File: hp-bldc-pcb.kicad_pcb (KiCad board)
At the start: 4 copper layers, 96 x 53 mm, 596 parts, among them IC101 MCP1790-5002E/DB, IC401 PIC16F1936, IC601 BTN8962TA, IC631 BTN8962TA, IC661 BTN8962TA, T102 SBC817-40LT1G, T103 SBC817-40LT1G

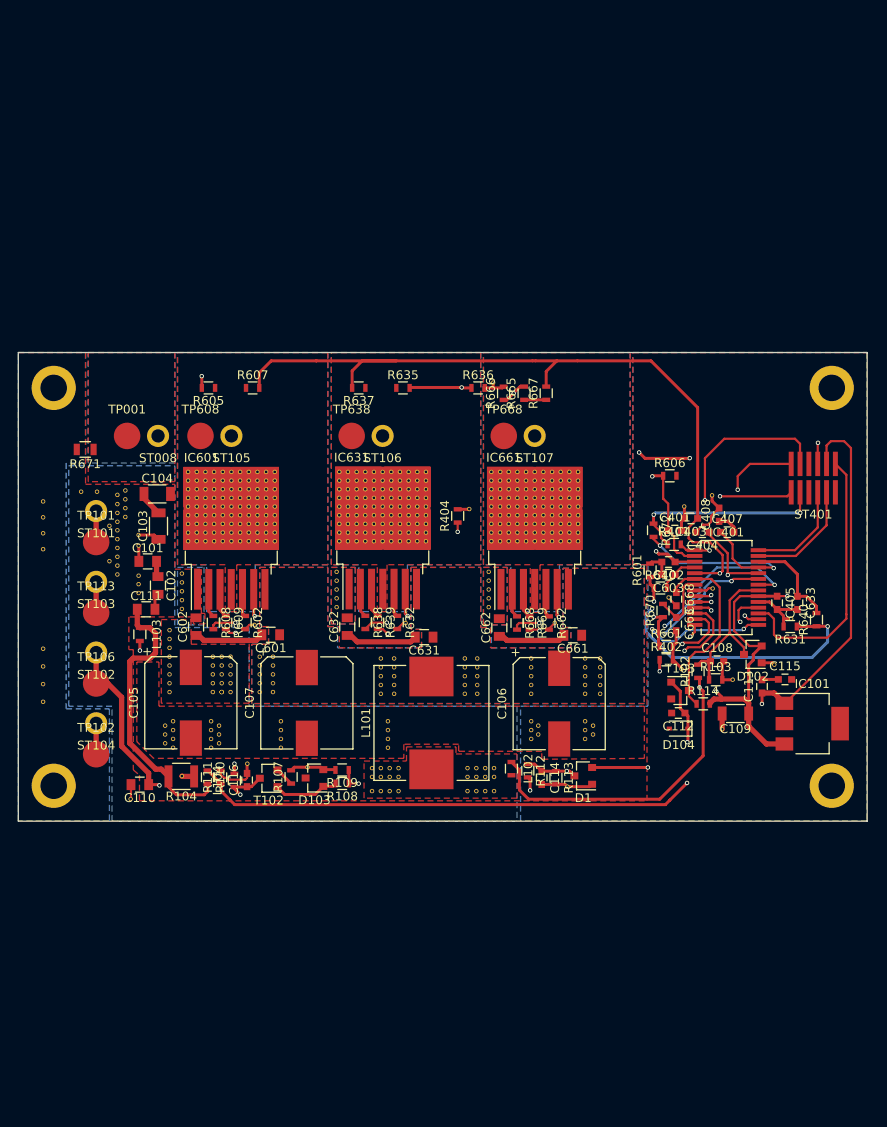
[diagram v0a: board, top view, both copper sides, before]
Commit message: - Finished adaptation to JMS board footprint. - Added testpoints. - Changed header connector to 0.1" pitch, and tall.
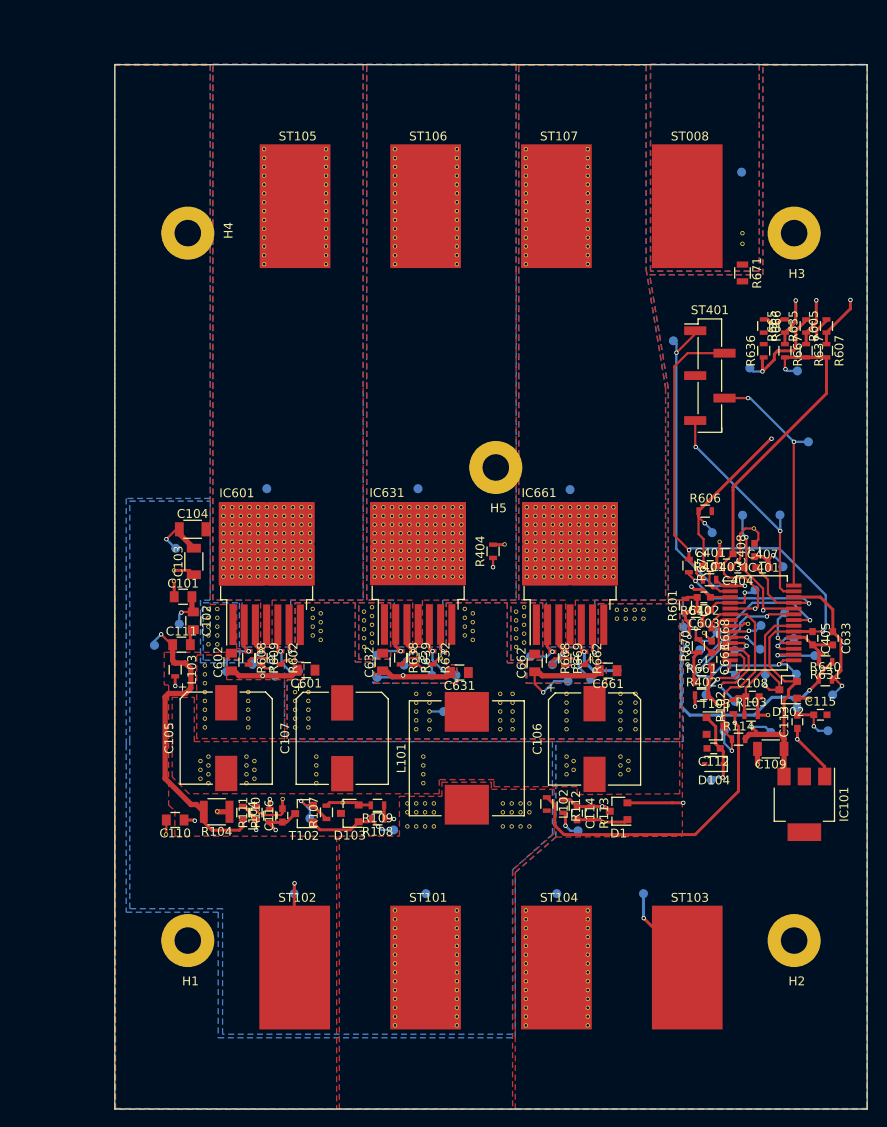
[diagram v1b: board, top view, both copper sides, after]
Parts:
- removed the REF** at (120.0, 107.4)
- removed the REF** at (119.0, 104.4)
- removed the REF** at (119.0, 103.4)
- removed the REF** at (107.2, 92.1)
- removed the REF** at (107.2, 91.1)
- removed the REF** at (107.2, 90.1)
- removed the REF** at (107.2, 89.1)
- removed the REF** at (107.2, 85.1)
- removed the REF** at (103.1, 84.7)
- removed the REF** at (109.6, 96.2)
- removed the REF** at (106.3, 88.6)
- removed the REF** at (109.6, 95.2)
- removed the REF** at (109.6, 94.2)
- removed the REF** at (106.3, 92.6)
- removed the REF** at (107.2, 94.1)
- removed the REF** at (149.7, 72.4)
- removed the REF** at (120.0, 106.4)
- removed the REF** at (108.1, 87.6)
- removed the REF** at (108.1, 86.6)
- removed the REF** at (108.1, 84.6)
- removed the REF** at (108.1, 85.6)
- removed the REF** at (120.0, 105.4)
- removed the REF** at (120.0, 104.4)
- removed the REF** at (120.0, 103.4)
- removed the REF** at (119.0, 107.4) (x2)
- removed the REF** at (98.8, 102.5)
- removed the REF** at (98.8, 104.5)
- removed the REF** at (98.8, 106.5)
- removed the REF** at (98.8, 108.5)
- removed the REF** at (98.8, 91.2)
- removed the REF** at (98.8, 89.4)
- removed the REF** at (98.8, 87.6)
- removed the REF** at (119.0, 106.4)
- removed the REF** at (98.8, 85.8)
- removed the REF** at (104.9, 84.7)
- removed the REF** at (107.2, 93.1)
- removed the REF** at (107.2, 86.1)
- removed the REF** at (107.2, 87.1)
- removed the REF** at (107.2, 88.1)
- removed the REF** at (119.0, 105.4)
- added H5: CONN_01X01, hp-bldc-pcb:ENCLOSURE_MOUNTING_HOLE, F.Cu at (150.0, 82.0)
- added REF**: VIA_0.3mm, hp-bldc-pcb:VIA_0.3mm, F.Cu at (177.9, 56.7)
- added REF**: VIA_0.3mm, hp-bldc-pcb:VIA_0.3mm, F.Cu at (163.7, 99.1)
- added REF**: VIA_0.3mm, hp-bldc-pcb:VIA_0.3mm, F.Cu at (160.4, 59.0)
- added REF**: VIA_0.3mm, hp-bldc-pcb:VIA_0.3mm, F.Cu at (153.4, 59.0)
- added REF**: VIA_0.3mm, hp-bldc-pcb:VIA_0.3mm, F.Cu at (160.4, 58.0)
- added REF**: VIA_0.3mm, hp-bldc-pcb:VIA_0.3mm, F.Cu at (153.4, 58.0)
- added REF**: VIA_0.3mm, hp-bldc-pcb:VIA_0.3mm, F.Cu at (160.4, 57.0)
- added REF**: VIA_0.3mm, hp-bldc-pcb:VIA_0.3mm, F.Cu at (153.4, 57.0)
- added REF**: VIA_0.3mm, hp-bldc-pcb:VIA_0.3mm, F.Cu at (160.4, 56.0)
- added REF**: VIA_0.3mm, hp-bldc-pcb:VIA_0.3mm, F.Cu at (153.4, 56.0)
- added REF**: VIA_0.3mm, hp-bldc-pcb:VIA_0.3mm, F.Cu at (160.4, 55.0)
- added REF**: VIA_0.3mm, hp-bldc-pcb:VIA_0.3mm, F.Cu at (153.4, 55.0)
- added REF**: VIA_0.3mm, hp-bldc-pcb:VIA_0.3mm, F.Cu at (163.7, 98.1)
- added REF**: VIA_0.3mm, hp-bldc-pcb:VIA_0.3mm, F.Cu at (160.4, 54.0)
- added REF**: VIA_0.3mm, hp-bldc-pcb:VIA_0.3mm, F.Cu at (153.4, 54.0)
- added REF**: VIA_0.3mm, hp-bldc-pcb:VIA_0.3mm, F.Cu at (160.4, 53.0)
- added REF**: VIA_0.3mm, hp-bldc-pcb:VIA_0.3mm, F.Cu at (153.4, 53.0)
- added REF**: VIA_0.3mm, hp-bldc-pcb:VIA_0.3mm, F.Cu at (160.4, 52.0)
- added REF**: VIA_0.3mm, hp-bldc-pcb:VIA_0.3mm, F.Cu at (153.4, 52.0)
- added REF**: VIA_0.3mm, hp-bldc-pcb:VIA_0.3mm, F.Cu at (160.4, 51.0)
- added REF**: VIA_0.3mm, hp-bldc-pcb:VIA_0.3mm, F.Cu at (153.4, 51.0)
- added REF**: VIA_0.3mm, hp-bldc-pcb:VIA_0.3mm, F.Cu at (160.4, 50.0)
- added REF**: VIA_0.3mm, hp-bldc-pcb:VIA_0.3mm, F.Cu at (153.4, 50.0)
- added REF**: VIA_0.3mm, hp-bldc-pcb:VIA_0.3mm, F.Cu at (147.4, 100.5)
- added REF**: VIA_0.3mm, hp-bldc-pcb:VIA_0.3mm, F.Cu at (160.4, 49.0)
- added REF**: VIA_0.3mm, hp-bldc-pcb:VIA_0.3mm, F.Cu at (153.4, 49.0)
- added REF**: VIA_0.3mm, hp-bldc-pcb:VIA_0.3mm, F.Cu at (160.4, 48.0)
- added REF**: VIA_0.3mm, hp-bldc-pcb:VIA_0.3mm, F.Cu at (153.4, 48.0)
- added REF**: VIA_0.3mm, hp-bldc-pcb:VIA_0.3mm, F.Cu at (160.4, 47.0)
- added REF**: VIA_0.3mm, hp-bldc-pcb:VIA_0.3mm, F.Cu at (153.4, 47.0)
- added REF**: VIA_0.3mm, hp-bldc-pcb:VIA_0.3mm, F.Cu at (160.4, 46.0)
- added REF**: VIA_0.3mm, hp-bldc-pcb:VIA_0.3mm, F.Cu at (153.4, 46.0)
- added REF**: VIA_0.3mm, hp-bldc-pcb:VIA_0.3mm, F.Cu at (145.6, 59.0)
- added REF**: VIA_0.3mm, hp-bldc-pcb:VIA_0.3mm, F.Cu at (138.6, 59.0)
- added REF**: VIA_0.3mm, hp-bldc-pcb:VIA_0.3mm, F.Cu at (147.4, 99.5)
- added REF**: VIA_0.3mm, hp-bldc-pcb:VIA_0.3mm, F.Cu at (145.6, 58.0)
- added REF**: VIA_0.3mm, hp-bldc-pcb:VIA_0.3mm, F.Cu at (138.6, 58.0)
- added REF**: VIA_0.3mm, hp-bldc-pcb:VIA_0.3mm, F.Cu at (145.6, 57.0)
- added REF**: VIA_0.3mm, hp-bldc-pcb:VIA_0.3mm, F.Cu at (138.6, 57.0)
- added REF**: VIA_0.3mm, hp-bldc-pcb:VIA_0.3mm, F.Cu at (145.6, 56.0)
- added REF**: VIA_0.3mm, hp-bldc-pcb:VIA_0.3mm, F.Cu at (138.6, 56.0)
- added REF**: VIA_0.3mm, hp-bldc-pcb:VIA_0.3mm, F.Cu at (145.6, 55.0)
- added REF**: VIA_0.3mm, hp-bldc-pcb:VIA_0.3mm, F.Cu at (138.6, 55.0)
- added REF**: VIA_0.3mm, hp-bldc-pcb:VIA_0.3mm, F.Cu at (145.6, 54.0)
- added REF**: VIA_0.3mm, hp-bldc-pcb:VIA_0.3mm, F.Cu at (138.6, 54.0)
- added REF**: VIA_0.3mm, hp-bldc-pcb:VIA_0.3mm, F.Cu at (147.4, 101.5)
- added REF**: VIA_0.3mm, hp-bldc-pcb:VIA_0.3mm, F.Cu at (145.6, 53.0)
- added REF**: VIA_0.3mm, hp-bldc-pcb:VIA_0.3mm, F.Cu at (138.6, 53.0)
- added REF**: VIA_0.3mm, hp-bldc-pcb:VIA_0.3mm, F.Cu at (145.6, 52.0)
- added REF**: VIA_0.3mm, hp-bldc-pcb:VIA_0.3mm, F.Cu at (138.6, 52.0)
- added REF**: VIA_0.3mm, hp-bldc-pcb:VIA_0.3mm, F.Cu at (145.6, 51.0)
- added REF**: VIA_0.3mm, hp-bldc-pcb:VIA_0.3mm, F.Cu at (138.6, 51.0)
- added REF**: VIA_0.3mm, hp-bldc-pcb:VIA_0.3mm, F.Cu at (145.6, 50.0)
- added REF**: VIA_0.3mm, hp-bldc-pcb:VIA_0.3mm, F.Cu at (138.6, 50.0)
- added REF**: VIA_0.3mm, hp-bldc-pcb:VIA_0.3mm, F.Cu at (145.6, 49.0)
- added REF**: VIA_0.3mm, hp-bldc-pcb:VIA_0.3mm, F.Cu at (138.6, 49.0)
- added REF**: VIA_0.3mm, hp-bldc-pcb:VIA_0.3mm, F.Cu at (147.4, 98.5)
- added REF**: VIA_0.3mm, hp-bldc-pcb:VIA_0.3mm, F.Cu at (145.6, 48.0)
- added REF**: VIA_0.3mm, hp-bldc-pcb:VIA_0.3mm, F.Cu at (138.6, 48.0)
- added REF**: VIA_0.3mm, hp-bldc-pcb:VIA_0.3mm, F.Cu at (145.6, 47.0)
- added REF**: VIA_0.3mm, hp-bldc-pcb:VIA_0.3mm, F.Cu at (138.6, 47.0)
- added REF**: VIA_0.3mm, hp-bldc-pcb:VIA_0.3mm, F.Cu at (145.6, 46.0)
- added REF**: VIA_0.3mm, hp-bldc-pcb:VIA_0.3mm, F.Cu at (138.6, 46.0)
- added REF**: VIA_0.3mm, hp-bldc-pcb:VIA_0.3mm, F.Cu at (130.8, 59.0)
- added REF**: VIA_0.3mm, hp-bldc-pcb:VIA_0.3mm, F.Cu at (123.8, 59.0)
- added REF**: VIA_0.3mm, hp-bldc-pcb:VIA_0.3mm, F.Cu at (130.8, 58.0)
- added REF**: VIA_0.3mm, hp-bldc-pcb:VIA_0.3mm, F.Cu at (123.8, 58.0)
- added REF**: VIA_0.3mm, hp-bldc-pcb:VIA_0.3mm, F.Cu at (146.5, 101.0)
- added REF**: VIA_0.3mm, hp-bldc-pcb:VIA_0.3mm, F.Cu at (130.8, 57.0)
- added REF**: VIA_0.3mm, hp-bldc-pcb:VIA_0.3mm, F.Cu at (123.8, 57.0)
- added REF**: VIA_0.3mm, hp-bldc-pcb:VIA_0.3mm, F.Cu at (130.8, 56.0)
- added REF**: VIA_0.3mm, hp-bldc-pcb:VIA_0.3mm, F.Cu at (123.8, 56.0)
- added REF**: VIA_0.3mm, hp-bldc-pcb:VIA_0.3mm, F.Cu at (130.8, 55.0)
- added REF**: VIA_0.3mm, hp-bldc-pcb:VIA_0.3mm, F.Cu at (123.8, 55.0)
- added REF**: VIA_0.3mm, hp-bldc-pcb:VIA_0.3mm, F.Cu at (130.8, 54.0)
- added REF**: VIA_0.3mm, hp-bldc-pcb:VIA_0.3mm, F.Cu at (123.8, 54.0)
- added REF**: VIA_0.3mm, hp-bldc-pcb:VIA_0.3mm, F.Cu at (130.8, 53.0)
- added REF**: VIA_0.3mm, hp-bldc-pcb:VIA_0.3mm, F.Cu at (123.8, 53.0)
- added REF**: VIA_0.3mm, hp-bldc-pcb:VIA_0.3mm, F.Cu at (146.5, 100.0)
- added REF**: VIA_0.3mm, hp-bldc-pcb:VIA_0.3mm, F.Cu at (130.8, 52.0)
- added REF**: VIA_0.3mm, hp-bldc-pcb:VIA_0.3mm, F.Cu at (123.8, 52.0)
- added REF**: VIA_0.3mm, hp-bldc-pcb:VIA_0.3mm, F.Cu at (130.8, 51.0)
- added REF**: VIA_0.3mm, hp-bldc-pcb:VIA_0.3mm, F.Cu at (123.8, 51.0)
- added REF**: VIA_0.3mm, hp-bldc-pcb:VIA_0.3mm, F.Cu at (130.8, 50.0)
- added REF**: VIA_0.3mm, hp-bldc-pcb:VIA_0.3mm, F.Cu at (123.8, 50.0)
- added REF**: VIA_0.3mm, hp-bldc-pcb:VIA_0.3mm, F.Cu at (130.8, 49.0)
- added REF**: VIA_0.3mm, hp-bldc-pcb:VIA_0.3mm, F.Cu at (123.8, 49.0)
- added REF**: VIA_0.3mm, hp-bldc-pcb:VIA_0.3mm, F.Cu at (130.8, 48.0)
- added REF**: VIA_0.3mm, hp-bldc-pcb:VIA_0.3mm, F.Cu at (123.8, 48.0)
- added REF**: VIA_0.3mm, hp-bldc-pcb:VIA_0.3mm, F.Cu at (146.5, 99.0)
- added REF**: VIA_0.3mm, hp-bldc-pcb:VIA_0.3mm, F.Cu at (130.8, 47.0)
- added REF**: VIA_0.3mm, hp-bldc-pcb:VIA_0.3mm, F.Cu at (123.8, 47.0)
- added REF**: VIA_0.3mm, hp-bldc-pcb:VIA_0.3mm, F.Cu at (130.8, 46.0)
- added REF**: VIA_0.3mm, hp-bldc-pcb:VIA_0.3mm, F.Cu at (123.8, 46.0)
- added REF**: VIA_0.3mm, hp-bldc-pcb:VIA_0.3mm, F.Cu at (146.5, 98.0)
- added REF**: VIA_0.3mm, hp-bldc-pcb:VIA_0.3mm, F.Cu at (177.9, 55.5)
- added REF**: VIA_0.3mm, hp-bldc-pcb:VIA_0.3mm, F.Cu at (130.2, 101.5)
- added REF**: VIA_0.3mm, hp-bldc-pcb:VIA_0.3mm, F.Cu at (130.2, 100.5)
- added REF**: VIA_0.3mm, hp-bldc-pcb:VIA_0.3mm, F.Cu at (130.2, 99.5)
- added REF**: VIA_0.3mm, hp-bldc-pcb:VIA_0.3mm, F.Cu at (130.2, 98.5)
- added REF**: VIA_0.3mm, hp-bldc-pcb:VIA_0.3mm, F.Cu at (129.3, 101.0)
- added REF**: VIA_0.3mm, hp-bldc-pcb:VIA_0.3mm, F.Cu at (129.3, 100.0)
- added REF**: VIA_0.3mm, hp-bldc-pcb:VIA_0.3mm, F.Cu at (129.3, 99.0)
- added REF**: VIA_0.3mm, hp-bldc-pcb:VIA_0.3mm, F.Cu at (129.3, 98.0)
- added REF**: VIA_0.3mm, hp-bldc-pcb:VIA_0.3mm, F.Cu at (152.3, 102.3)
- added REF**: VIA_0.3mm, hp-bldc-pcb:VIA_0.3mm, F.Cu at (152.3, 101.3)
- added REF**: VIA_0.3mm, hp-bldc-pcb:VIA_0.3mm, F.Cu at (152.3, 100.3)
- added REF**: VIA_0.3mm, hp-bldc-pcb:VIA_0.3mm, F.Cu at (152.3, 99.3)
- added REF**: VIA_0.3mm, hp-bldc-pcb:VIA_0.3mm, F.Cu at (152.3, 98.3)
- added REF**: VIA_0.3mm, hp-bldc-pcb:VIA_0.3mm, F.Cu at (117.5, 102.0)
- added REF**: VIA_0.3mm, hp-bldc-pcb:VIA_0.3mm, F.Cu at (117.5, 101.0)
- added REF**: VIA_0.3mm, hp-bldc-pcb:VIA_0.3mm, F.Cu at (117.5, 100.0)
- added REF**: VIA_0.3mm, hp-bldc-pcb:VIA_0.3mm, F.Cu at (117.5, 99.0)
- added REF**: VIA_0.3mm, hp-bldc-pcb:VIA_0.3mm, F.Cu at (117.5, 98.0)
- added REF**: VIA_0.3mm, hp-bldc-pcb:VIA_0.3mm, F.Cu at (135.1, 102.3)
- added REF**: VIA_0.3mm, hp-bldc-pcb:VIA_0.3mm, F.Cu at (135.1, 101.3)
- added REF**: VIA_0.3mm, hp-bldc-pcb:VIA_0.3mm, F.Cu at (166.7, 99.1)
- added REF**: VIA_0.3mm, hp-bldc-pcb:VIA_0.3mm, F.Cu at (135.1, 100.3)
- added REF**: VIA_0.3mm, hp-bldc-pcb:VIA_0.3mm, F.Cu at (135.1, 99.3)
- added REF**: VIA_0.3mm, hp-bldc-pcb:VIA_0.3mm, F.Cu at (135.1, 98.3)
- added REF**: VIA_0.3mm, hp-bldc-pcb:VIA_0.3mm, F.Cu at (160.4, 145.1)
- added REF**: VIA_0.3mm, hp-bldc-pcb:VIA_0.3mm, F.Cu at (153.4, 145.1)
- added REF**: VIA_0.3mm, hp-bldc-pcb:VIA_0.3mm, F.Cu at (160.4, 144.1)
- added REF**: VIA_0.3mm, hp-bldc-pcb:VIA_0.3mm, F.Cu at (153.4, 144.1)
- added REF**: VIA_0.3mm, hp-bldc-pcb:VIA_0.3mm, F.Cu at (160.4, 143.1)
- added REF**: VIA_0.3mm, hp-bldc-pcb:VIA_0.3mm, F.Cu at (153.4, 143.1)
- added REF**: VIA_0.3mm, hp-bldc-pcb:VIA_0.3mm, F.Cu at (166.7, 98.1)
- added REF**: VIA_0.3mm, hp-bldc-pcb:VIA_0.3mm, F.Cu at (160.4, 142.1)
- added REF**: VIA_0.3mm, hp-bldc-pcb:VIA_0.3mm, F.Cu at (153.4, 142.1)
- added REF**: VIA_0.3mm, hp-bldc-pcb:VIA_0.3mm, F.Cu at (160.4, 141.1)
- added REF**: VIA_0.3mm, hp-bldc-pcb:VIA_0.3mm, F.Cu at (153.4, 141.1)
- added REF**: VIA_0.3mm, hp-bldc-pcb:VIA_0.3mm, F.Cu at (160.4, 140.1)
- added REF**: VIA_0.3mm, hp-bldc-pcb:VIA_0.3mm, F.Cu at (153.4, 140.1)
- added REF**: VIA_0.3mm, hp-bldc-pcb:VIA_0.3mm, F.Cu at (160.4, 139.1)
- added REF**: VIA_0.3mm, hp-bldc-pcb:VIA_0.3mm, F.Cu at (153.4, 139.1)
- added REF**: VIA_0.3mm, hp-bldc-pcb:VIA_0.3mm, F.Cu at (160.4, 138.1)
- added REF**: VIA_0.3mm, hp-bldc-pcb:VIA_0.3mm, F.Cu at (153.4, 138.1)
- added REF**: VIA_0.3mm, hp-bldc-pcb:VIA_0.3mm, F.Cu at (165.7, 99.1)
- added REF**: VIA_0.3mm, hp-bldc-pcb:VIA_0.3mm, F.Cu at (160.4, 137.1)
- added REF**: VIA_0.3mm, hp-bldc-pcb:VIA_0.3mm, F.Cu at (153.4, 137.1)
- added REF**: VIA_0.3mm, hp-bldc-pcb:VIA_0.3mm, F.Cu at (160.4, 136.1)
- added REF**: VIA_0.3mm, hp-bldc-pcb:VIA_0.3mm, F.Cu at (153.4, 136.1)
- added REF**: VIA_0.3mm, hp-bldc-pcb:VIA_0.3mm, F.Cu at (160.4, 135.1)
- added REF**: VIA_0.3mm, hp-bldc-pcb:VIA_0.3mm, F.Cu at (153.4, 135.1)
- added REF**: VIA_0.3mm, hp-bldc-pcb:VIA_0.3mm, F.Cu at (160.4, 134.1)
- added REF**: VIA_0.3mm, hp-bldc-pcb:VIA_0.3mm, F.Cu at (153.4, 134.1)
- added REF**: VIA_0.3mm, hp-bldc-pcb:VIA_0.3mm, F.Cu at (160.4, 133.1)
- added REF**: VIA_0.3mm, hp-bldc-pcb:VIA_0.3mm, F.Cu at (153.4, 133.1)
- added REF**: VIA_0.3mm, hp-bldc-pcb:VIA_0.3mm, F.Cu at (165.7, 98.1)
- added REF**: VIA_0.3mm, hp-bldc-pcb:VIA_0.3mm, F.Cu at (160.4, 132.1)
- added REF**: VIA_0.3mm, hp-bldc-pcb:VIA_0.3mm, F.Cu at (153.4, 132.1)
- added REF**: VIA_0.3mm, hp-bldc-pcb:VIA_0.3mm, F.Cu at (145.6, 145.1)
- added REF**: VIA_0.3mm, hp-bldc-pcb:VIA_0.3mm, F.Cu at (138.6, 145.1)
- added REF**: VIA_0.3mm, hp-bldc-pcb:VIA_0.3mm, F.Cu at (145.6, 144.1)
- added REF**: VIA_0.3mm, hp-bldc-pcb:VIA_0.3mm, F.Cu at (138.6, 144.1)
- added REF**: VIA_0.3mm, hp-bldc-pcb:VIA_0.3mm, F.Cu at (145.6, 143.1)
- added REF**: VIA_0.3mm, hp-bldc-pcb:VIA_0.3mm, F.Cu at (138.6, 143.1)
- added REF**: VIA_0.3mm, hp-bldc-pcb:VIA_0.3mm, F.Cu at (145.6, 142.1)
- added REF**: VIA_0.3mm, hp-bldc-pcb:VIA_0.3mm, F.Cu at (138.6, 142.1)
- added REF**: VIA_0.3mm, hp-bldc-pcb:VIA_0.3mm, F.Cu at (164.7, 99.1)
- added REF**: VIA_0.3mm, hp-bldc-pcb:VIA_0.3mm, F.Cu at (145.6, 141.1)
- added REF**: VIA_0.3mm, hp-bldc-pcb:VIA_0.3mm, F.Cu at (138.6, 141.1)
- added REF**: VIA_0.3mm, hp-bldc-pcb:VIA_0.3mm, F.Cu at (145.6, 140.1)
- added REF**: VIA_0.3mm, hp-bldc-pcb:VIA_0.3mm, F.Cu at (138.6, 140.1)
- added REF**: VIA_0.3mm, hp-bldc-pcb:VIA_0.3mm, F.Cu at (145.6, 139.1)
- added REF**: VIA_0.3mm, hp-bldc-pcb:VIA_0.3mm, F.Cu at (138.6, 139.1)
- added REF**: VIA_0.3mm, hp-bldc-pcb:VIA_0.3mm, F.Cu at (145.6, 138.1)
- added REF**: VIA_0.3mm, hp-bldc-pcb:VIA_0.3mm, F.Cu at (138.6, 138.1)
- added REF**: VIA_0.3mm, hp-bldc-pcb:VIA_0.3mm, F.Cu at (145.6, 137.1)
- added REF**: VIA_0.3mm, hp-bldc-pcb:VIA_0.3mm, F.Cu at (138.6, 137.1)
- added REF**: VIA_0.3mm, hp-bldc-pcb:VIA_0.3mm, F.Cu at (164.7, 98.1)
- added REF**: VIA_0.3mm, hp-bldc-pcb:VIA_0.3mm, F.Cu at (145.6, 136.1)
- added REF**: VIA_0.3mm, hp-bldc-pcb:VIA_0.3mm, F.Cu at (138.6, 136.1)
- added REF**: VIA_0.3mm, hp-bldc-pcb:VIA_0.3mm, F.Cu at (145.6, 135.1)
- added REF**: VIA_0.3mm, hp-bldc-pcb:VIA_0.3mm, F.Cu at (138.6, 135.1)
- added REF**: VIA_0.3mm, hp-bldc-pcb:VIA_0.3mm, F.Cu at (145.6, 134.1)
- added REF**: VIA_0.3mm, hp-bldc-pcb:VIA_0.3mm, F.Cu at (138.6, 134.1)
- added REF**: VIA_0.3mm, hp-bldc-pcb:VIA_0.3mm, F.Cu at (145.6, 133.1)
- added REF**: VIA_0.3mm, hp-bldc-pcb:VIA_0.3mm, F.Cu at (138.6, 133.1)
- added REF**: VIA_0.3mm, hp-bldc-pcb:VIA_0.3mm, F.Cu at (145.6, 132.1)
- added REF**: VIA_0.3mm, hp-bldc-pcb:VIA_0.3mm, F.Cu at (138.6, 132.1)
- added TP104: TEST, hp-bldc-pcb:TEST_POINT_40mil, B.Cu at (113.8, 91.1)
- added TP105: TEST, hp-bldc-pcb:TEST_POINT_40mil, B.Cu at (144.1, 109.6)
- added TP107: TEST, hp-bldc-pcb:TEST_POINT_40mil, B.Cu at (181.1, 112.0)
- added TP108: TEST, hp-bldc-pcb:TEST_POINT_40mil, B.Cu at (127.2, 130.2)
- added TP109: TEST, hp-bldc-pcb:TEST_POINT_40mil, B.Cu at (159.3, 123.1)
- added TP110: TEST, hp-bldc-pcb:TEST_POINT_40mil, B.Cu at (129.0, 121.7)
- added TP111: TEST, hp-bldc-pcb:TEST_POINT_40mil, B.Cu at (138.4, 123.0)
- added TP112: TEST, hp-bldc-pcb:TEST_POINT_40mil, B.Cu at (177.0, 102.7)
- added TP114: TEST, hp-bldc-pcb:TEST_POINT_40mil, B.Cu at (175.8, 111.8)
- added TP116: TEST, hp-bldc-pcb:TEST_POINT_40mil, B.Cu at (114.2, 99.7)
- added TP117: TEST, hp-bldc-pcb:TEST_POINT_40mil, B.Cu at (179.9, 102.5)
- added TP118: TEST, hp-bldc-pcb:TEST_POINT_40mil, B.Cu at (187.6, 111.8)
- added TP119: TEST, hp-bldc-pcb:TEST_POINT_40mil, B.Cu at (174.4, 117.3)
- added TP401: TEST, hp-bldc-pcb:TEST_POINT_40mil, B.Cu at (170.1, 67.7)
- added TP402: TEST, hp-bldc-pcb:TEST_POINT_40mil, B.Cu at (184.1, 71.1)
- added TP404: TEST, hp-bldc-pcb:TEST_POINT_40mil, B.Cu at (182.5, 93.2)
- added TP405: TEST, hp-bldc-pcb:TEST_POINT_40mil, B.Cu at (186.1, 103.3)
- added TP406: TEST, hp-bldc-pcb:TEST_POINT_40mil, B.Cu at (183.7, 101.3)
- added TP407: TEST, hp-bldc-pcb:TEST_POINT_40mil, B.Cu at (182.7, 98.4)
- added TP408: TEST, hp-bldc-pcb:TEST_POINT_40mil, B.Cu at (180.0, 99.9)
- added TP409: TEST, hp-bldc-pcb:TEST_POINT_40mil, B.Cu at (185.3, 79.1)
- added TP410: TEST, hp-bldc-pcb:TEST_POINT_40mil, B.Cu at (182.1, 87.4)
- added TP601: TEST, hp-bldc-pcb:TEST_POINT_40mil, B.Cu at (125.0, 105.6)
- added TP602: TEST, hp-bldc-pcb:TEST_POINT_40mil, B.Cu at (173.8, 107.7)
- added TP603: TEST, hp-bldc-pcb:TEST_POINT_40mil, B.Cu at (179.3, 95.9)
- added TP604: TEST, hp-bldc-pcb:TEST_POINT_40mil, B.Cu at (177.1, 108.5)
- added TP605: TEST, hp-bldc-pcb:TEST_POINT_40mil, B.Cu at (127.7, 105.0)
- added TP609: TEST, hp-bldc-pcb:TEST_POINT_40mil, B.Cu at (174.5, 89.4)
- added TP610: TEST, hp-bldc-pcb:TEST_POINT_40mil, B.Cu at (119.6, 105.1)
- added TP611: TEST, hp-bldc-pcb:TEST_POINT_40mil, B.Cu at (122.5, 104.3)
- added TP612: TEST, hp-bldc-pcb:TEST_POINT_40mil, B.Cu at (171.2, 100.0)
- added TP631: TEST, hp-bldc-pcb:TEST_POINT_40mil, B.Cu at (136.6, 105.7)
- added TP632: TEST, hp-bldc-pcb:TEST_POINT_40mil, B.Cu at (142.8, 105.5)
- added TP633: TEST, hp-bldc-pcb:TEST_POINT_40mil, B.Cu at (188.1, 107.7)
- added TP634: TEST, hp-bldc-pcb:TEST_POINT_40mil, B.Cu at (177.1, 105.5)
- added TP635: TEST, hp-bldc-pcb:TEST_POINT_40mil, B.Cu at (145.5, 105.5)
- added TP639: TEST, hp-bldc-pcb:TEST_POINT_40mil, B.Cu at (178.7, 70.8)
- added TP640: TEST, hp-bldc-pcb:TEST_POINT_40mil, B.Cu at (136.6, 103.2)
- added TP641: TEST, hp-bldc-pcb:TEST_POINT_40mil, B.Cu at (139.6, 104.3)
- added TP642: TEST, hp-bldc-pcb:TEST_POINT_40mil, B.Cu at (184.1, 109.2)
- added TP661: TEST, hp-bldc-pcb:TEST_POINT_40mil, B.Cu at (158.2, 106.2)
- added TP662: TEST, hp-bldc-pcb:TEST_POINT_40mil, B.Cu at (160.7, 105.9)
- added TP663: TEST, hp-bldc-pcb:TEST_POINT_40mil, B.Cu at (175.0, 100.6)
- added TP664: TEST, hp-bldc-pcb:TEST_POINT_40mil, B.Cu at (184.0, 105.4)
- added TP665: TEST, hp-bldc-pcb:TEST_POINT_40mil, B.Cu at (163.7, 105.0)
- added TP669: TEST, hp-bldc-pcb:TEST_POINT_40mil, B.Cu at (177.9, 87.4)
- added TP670: TEST, hp-bldc-pcb:TEST_POINT_40mil, B.Cu at (153.9, 103.4)
- added TP671: TEST, hp-bldc-pcb:TEST_POINT_40mil, B.Cu at (156.4, 104.3)
- added TP672: TEST, hp-bldc-pcb:TEST_POINT_40mil, B.Cu at (173.1, 102.6)
- added TP673: TEST, hp-bldc-pcb:TEST_POINT_40mil, B.Cu at (111.4, 102.1)
- H1, H2, H3, H4: footprint hp-bldc-pcb:MOUNTING_HOLE_FOR_4-40 -> hp-bldc-pcb:ENCLOSURE_MOUNTING_HOLE
- ST008, ST101, ST102, ST103, ST104, ST105, ST106, ST107: footprint hp-bldc-pcb:WIRE_HARNESS_THRU_HOLE -> hp-bldc-pcb:BIG_RECT_PAD
- ST401: value CONN_02X06 -> CONN_01X05; footprint hp-bldc-pcb:HEADER_CONN_(FTM-106-02-L-DV) -> Pin_Headers:Pin_Header_Straight_1x05_Pitch2.54mm_SMD_Pin1Left
- TP001, TP101, TP102, TP106, TP113, TP608, TP638, TP668: footprint Measurement_Points:Measurement_Point_Round-SMD-Pad_Big -> hp-bldc-pcb:TEST_POINT_40mil; moved to B.Cu
- moved ST103 79.8 mm to (171.7, 138.6)
- moved R671 77.0 mm to (177.9, 60.0), turned to 270 degrees
- moved TP106 75.7 mm to (180.5, 105.4)
- moved TP001 75.6 mm to (177.8, 48.6)
- moved R605 70.2 mm to (187.4, 66.0), turned to 90 degrees
- moved TP113 69.6 mm to (166.7, 130.2)
- moved ST008 65.3 mm to (171.7, 52.4)
- moved R607 65.0 mm to (187.4, 68.8), turned to 270 degrees
- moved ST101 63.7 mm to (142.1, 138.6)
- moved ST104 58.9 mm to (156.9, 138.6)
- moved TP101 54.5 mm to (142.1, 130.2)
- moved TP102 54.4 mm to (156.9, 130.2)
- moved R637 50.8 mm to (185.1, 68.8), turned to 270 degrees
- moved R635 46.1 mm to (185.1, 66.0), turned to 90 degrees
- moved ST102 42.1 mm to (127.3, 138.6)
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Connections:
- ST401 pad 2: Net-(IC401-Pad18) -> 5V
- ST401 pad 3: 5V -> Earth
- ST401 pad 4: Net-(IC401-Pad9) -> Net-(IC401-Pad28)
- ST401 pad 5: Earth -> Net-(IC401-Pad27)
- TP106 pad 1: DIAG -> VBATT_SENSE
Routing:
- net PH_1: track 0.00 -> 100.4 mm, vias 0 -> 1
- net PH_2: track 0.00 -> 84.8 mm, vias 0 -> 1
- net CMD: track 14.4 -> 85.1 mm, vias 1 -> 2
- net PH_3: track 2.50 -> 69.3 mm, vias 0 -> 1
- net PH_SUM_SENSE: track 107.7 -> 64.4 mm, vias 2 -> 3
- net VBATT_2: track 85.3 -> 50.4 mm
- net PH_1_V_SENSE: track 77.2 -> 42.3 mm, vias 2 -> 3
- net Net-(IC401-Pad9): track 32.1 -> 3.89 mm, vias 2 -> 1
- net Net-(IC401-Pad17): track 31.1 -> 4.13 mm, vias 0 -> 1
- net Net-(IC401-Pad16): track 30.7 -> 6.08 mm, vias 2 -> 1
- net Net-(IC401-Pad18): track 27.0 -> 5.21 mm, vias 2 -> 1
- net Net-(IC401-Pad1): track 18.4 -> 40.1 mm
- net 5V: track 91.6 -> 111.6 mm, vias 5 -> 4
- net Net-(IC401-Pad28): track 11.7 -> 27.8 mm, vias 0 -> 2
- net Net-(IC401-Pad27): track 12.9 -> 26.5 mm, vias 0 -> 2
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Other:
- board size 96 x 53 mm -> 85.1 x 118.1 mm
- board text added: "HP BLDC PCB, v1.0 TI AUTOMOTIVE, 3/18"
- board text removed: "HP BLDC PCB, v1.0 TI AUTOMOTIVE, 2/18"

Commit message: - Minor changes to silkscreen. - Minor changes to BOM. - Additions to Readme file. - Page layout changed in schematic.
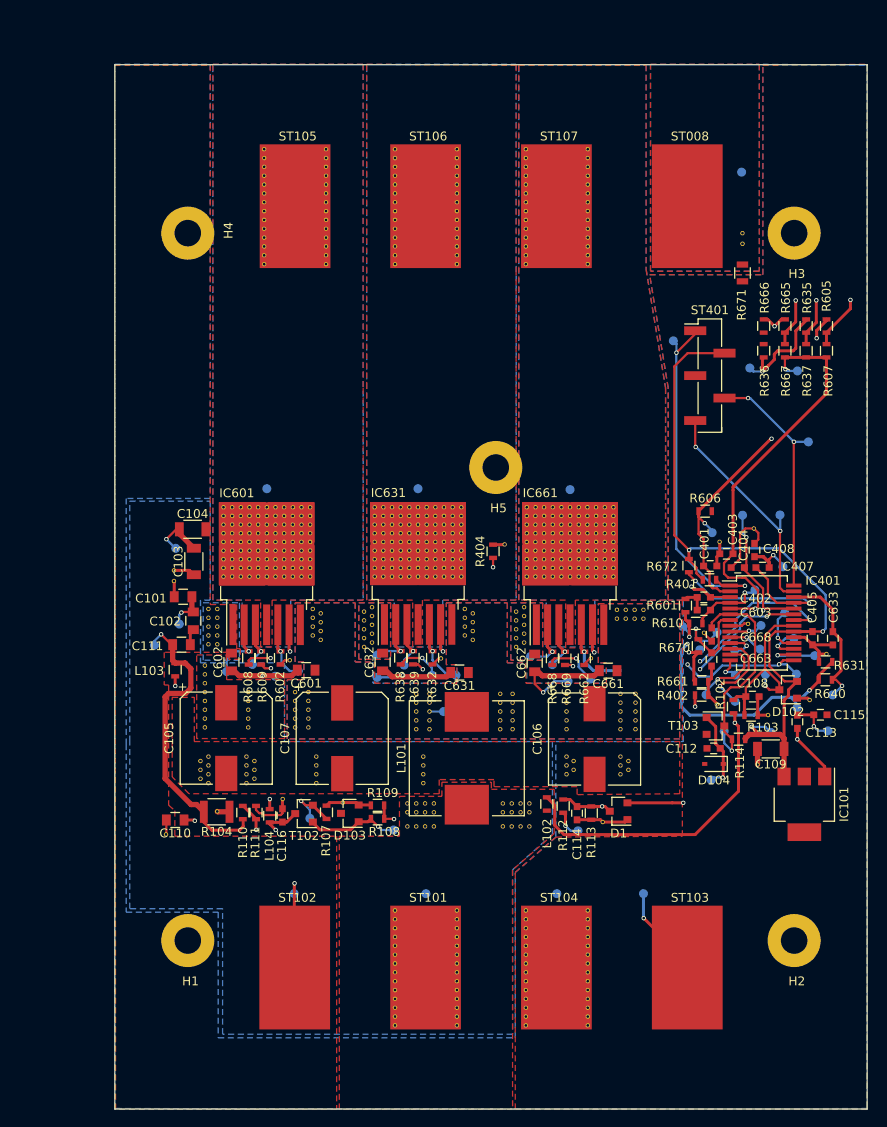
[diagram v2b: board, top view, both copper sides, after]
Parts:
- IC101: footprint TO_SOT_Packages_SMD:SOT-223 -> hp-bldc-pcb:SOT-223
- IC601, IC631, IC661: footprint TO_SOT_Packages_SMD:TO-263-7_TabPin8 -> hp-bldc-pcb:TO-263-7_TabPin8
- L101: footprint Inductors_SMD:L_Wuerth_HCI-1365 -> hp-bldc-pcb:L_Wuerth_HCI-1365
- ST401: footprint Pin_Headers:Pin_Header_Straight_1x05_Pitch2.54mm_SMD_Pin1Left -> hp-bldc-pcb:Pin_Header_Straight_1x05_Pitch2.54mm_SMD_Pin1Left
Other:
- board text added: "COMMAND"
- board text added: "DIAGNOSTIC"
- board text added: "GROUND"
- board text added: "HP BLDC PCB, v1.0 TI AUTOMOTIVE, 5/18"
- board text added: "PHASE_1"
- board text added: "PHASE_2"
- board text added: "PHASE_3"
- board text added: "PUMP_GND"
- board text added: "VBATT"
- board text removed: "HP BLDC PCB, v1.0 TI AUTOMOTIVE, 3/18"

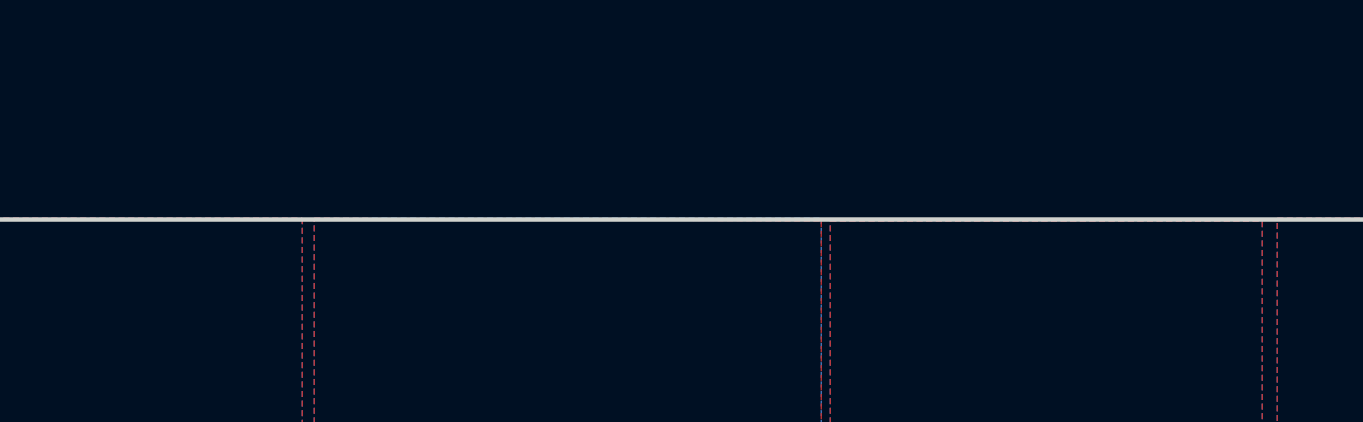
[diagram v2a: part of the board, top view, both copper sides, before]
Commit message: -Changed naming convention of gerber zip file.
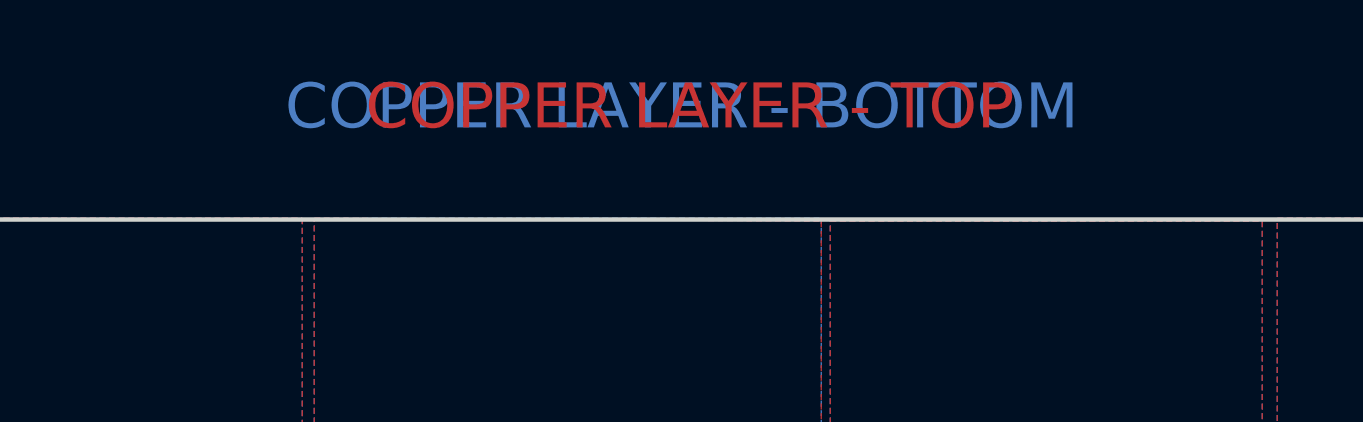
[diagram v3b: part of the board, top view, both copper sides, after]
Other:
- board text added: "COPPER LAYER - BOTTOM"
- board text added: "COPPER LAYER - IN1"
- board text added: "COPPER LAYER - IN2"
- board text added: "COPPER LAYER - TOP"
- board text added: "SOLDER MASK - BOTTOM"
- board text added: "SOLDER MASK - TOP"
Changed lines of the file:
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@@
     (links 880)
     (no_connects 0)
-    (area 103.121907 36.369844 192.178572 154.630181)
+    (area 103.121907 31.48 192.178572 154.630181)
     (thickness 1.6)
-    (drawings 12363)
+    (drawings 12369)
     (tracks 892)
     (zones 0)
@@
     (nets 63)
   )
-  (page A4)
+  (page USLetter)
+  (title_block
+    (title HP_BLDC_PCB)
+    (date 5/18)
+    (rev v1.0)
+  )
   (layers
     (0 F.Cu signal)
@@
     )
   )
+  (gr_text "SOLDER MASK - BOTTOM" (at 146.94 32.77) (layer B.Mask)
+    (effects (font (size 1.5 1.5) (thickness 0.3)))
+  )
+  (gr_text "SOLDER MASK - TOP" (at 147.74 32.68) (layer F.Mask)
+    (effects (font (size 1.5 1.5) (thickness 0.3)))
+  )
+  (gr_text "COPPER LAYER - BOTTOM" (at 147.65 32.68) (layer B.Cu)
+    (effects (font (size 1.5 1.5) (thickness 0.3)))
+  )
+  (gr_text "COPPER LAYER - IN2" (at 147.74 32.77) (layer In2.Cu)
+    (effects (font (size 1.5 1.5) (thickness 0.3)))
+  )
+  (gr_text "COPPER LAYER - IN1" (at 147.65 32.68) (layer In1.Cu)
+    (effects (font (size 1.5 1.5) (thickness 0.3)))
+  )
+  (gr_text "COPPER LAYER - TOP" (at 147.92 32.68) (layer F.Cu)
+    (effects (font (size 1.5 1.5) (thickness 0.3)))
+  )
   (gr_text PUMP_GND (at 171.75 62 180) (layer Cmts.User)

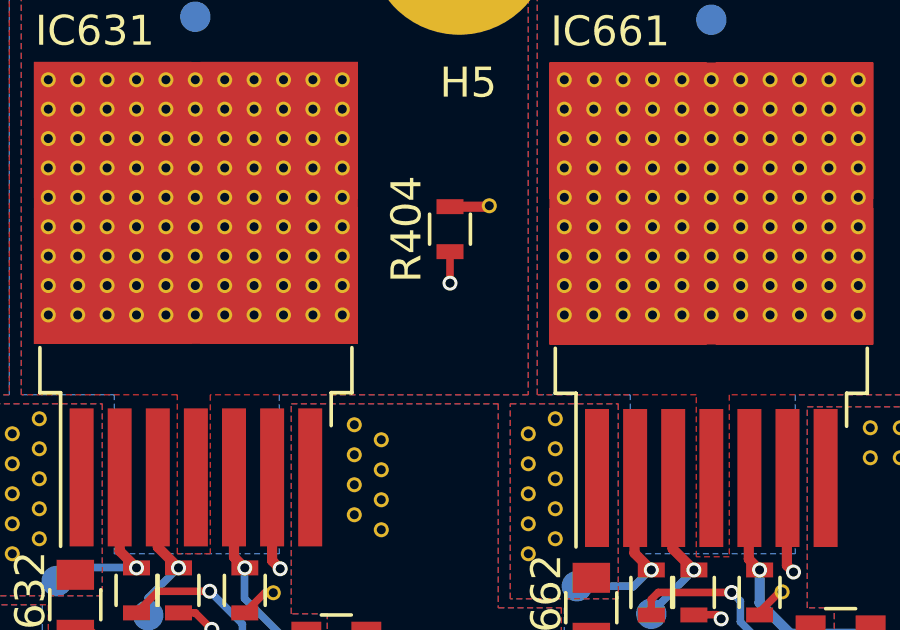
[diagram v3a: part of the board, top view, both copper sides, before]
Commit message: - Added TP411 at JMS request.  This was needed to test the NTC during ICT.
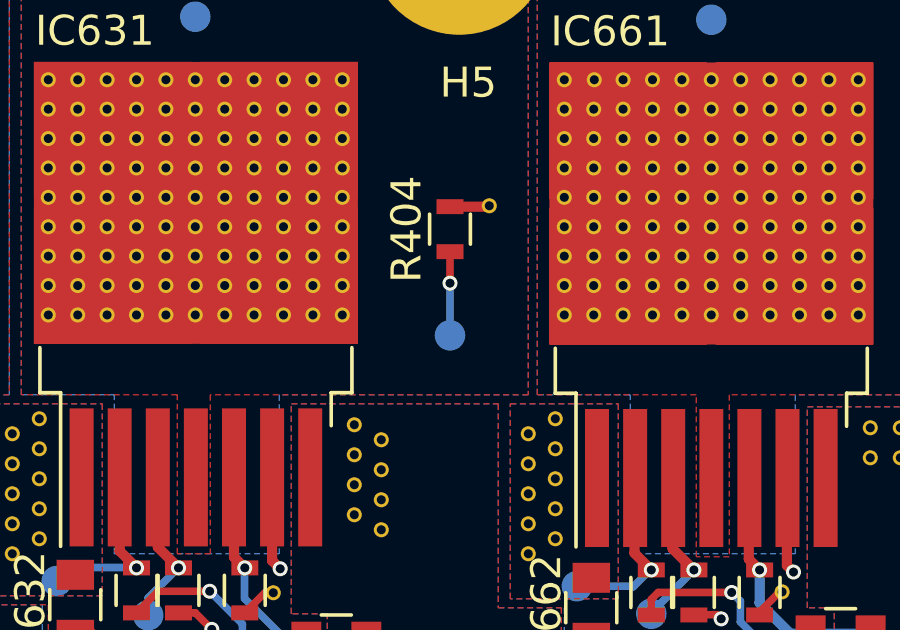
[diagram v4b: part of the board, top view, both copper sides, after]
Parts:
- added TP411: TEST, hp-bldc-pcb:TEST_POINT_40mil, B.Cu at (149.7, 95.0)
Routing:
- net Net-(C407-Pad1): track 58.0 -> 59.7 mm
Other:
- board text added: "HP BLDC PCB, v1.1 TI AUTOMOTIVE, 10/18"
- board text removed: "HP BLDC PCB, v1.0 TI AUTOMOTIVE, 5/18"
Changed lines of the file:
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@@
 (kicad_pcb (version 4) (host pcbnew 4.0.6)
   (general
-    (links 880)
+    (links 881)
     (no_connects 0)
     (area 103.121907 31.48 192.178572 154.630181)
     (thickness 1.6)
     (drawings 12369)
-    (tracks 892)
+    (tracks 893)
     (zones 0)
-    (modules 787)
+    (modules 788)
     (nets 63)
   )
@@
     (pad_to_mask_clearance 0.2)
     (aux_axis_origin 0 0)
-    (visible_elements 7FFEF77F)
+    (visible_elements 7FFEFF7F)
     (pcbplotparams
-      (layerselection 0x012fc_80000007)
+      (layerselection 0x010cc_80000007)
       (usegerberextensions false)
       (excludeedgelayer true)
@@
     )
   )
+  (module hp-bldc-pcb:TEST_POINT_40mil (layer B.Cu)
+    (at 149.69 95.02)
+    (fp_text reference TP411 (at -0.11 1.53) (layer B.SilkS)
+      (effects (font (size 1 1) (thickness 0.15)) (justify mirror))
+    )
+    (fp_text value TEST (at 0 1.3) (layer B.Fab) hide
+      (effects (font (size 1 1) (thickness 0.15)) (justify mirror))
+    )
+    (pad 1 smd circle (at 0 0) (size 1.016 1.016) (layers B.Cu B.Mask)
+      (net 20 "Net-(C407-Pad1)"))
+  )
   (gr_text "SOLDER MASK - BOTTOM" (at 146.94 32.77) (layer B.Mask)
     (effects (font (size 1.5 1.5) (thickness 0.3)))
@@
     (effects (font (size 0.7 0.7) (thickness 0.1)))
   )
-  (gr_text "HP BLDC PCB, v1.0\nTI AUTOMOTIVE, 5/18" (at 179.5 152.3) (layer Cmts.User)
+  (gr_text "HP BLDC PCB, v1.1\nTI AUTOMOTIVE, 10/18" (at 179.21 152.27) (layer Cmts.User)
     (effects (font (size 0.7 0.7) (thickness 0.1)) (justify left))
   )
@@
   (segment (start 180.26 92.09) (end 179.26 92.09) (width 0.381) (layer F.Cu) (net 19))
   (segment (start 180.92 92.75) (end 180.26 92.09) (width 0.381) (layer F.Cu) (net 19))
+  (segment (start 149.69 95.02) (end 149.69 93.28) (width 0.25) (layer B.Cu) (net 20))
   (segment (start 149.69 93.28) (end 149.69 94.69) (width 0.34) (layer In2.Cu) (net 20))
   (via (at 149.69 93.28) (size 0.5) (drill 0.3) (layers F.Cu B.Cu) (net 20))
